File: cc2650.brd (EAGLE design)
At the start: 50.8 x 22.9 mm, 22 parts, among them IC1 TPS73133DBVR, IC4 CC2650MODAMOHR, SW1 SPST_TACT-KMR2, SW3 SPST_TACT-KMR2

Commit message: changed resistor values for LEDS.
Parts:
- LED2: value RED -> GREEN
- R2: value 470 -> 715
- R3: value 470 -> 787
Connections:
- removed net N$4: JP2.1
- net DIO5_TDO: now also JP2.1
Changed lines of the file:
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@@
 <attribute name="VALUE" x="19.134" y="20.334" size="0.4064" layer="27" rot="R180"/>
 </element>
-<element name="R3" library="adafruit" package="R1206" value="470" x="15.8115" y="12.065" rot="MR90">
+<element name="R3" library="adafruit" package="R1206" value="787" x="15.8115" y="12.065" rot="MR90">
 <attribute name="MF" value="" x="15.8115" y="12.065" size="1.778" layer="28" rot="MR90" display="off"/>
 <attribute name="MPN" value="CR1206-FX-4700ELF" x="15.8115" y="12.065" size="1.778" layer="28" rot="MR90" display="off"/>
@@
 <element name="CN1" library="adafruit" package="JST-PH-2-THM-RA" value="" x="10.795" y="16.51"/>
 <element name="MS1" library="wing_modified" package="FEATHERWING_DIM" value="FEATHERWING_NODIM" x="0" y="0"/>
-<element name="R2" library="adafruit" package="R1206" value="470" x="18.415" y="12.065" rot="MR90">
+<element name="R2" library="adafruit" package="R1206" value="715" x="18.415" y="12.065" rot="MR90">
 <attribute name="MF" value="" x="36.195" y="12.065" size="1.778" layer="28" rot="MR90" display="off"/>
 <attribute name="MPN" value="CR1206-FX-4700ELF" x="36.195" y="12.065" size="1.778" layer="28" rot="MR90" display="off"/>
 <attribute name="OC_NEWARK" value="06X5194" x="36.195" y="12.065" size="1.778" layer="28" rot="MR90" display="off"/>
 </element>
-<element name="LED2" library="adafruit" package="CHIPLED_1206" value="RED" x="18.415" y="12.065" rot="R180">
+<element name="LED2" library="adafruit" package="CHIPLED_1206" value="GREEN" x="18.415" y="12.065" rot="R180">
 <attribute name="MF" value="" x="29.845" y="-6.35" size="1.778" layer="27" rot="R180" display="off"/>
 <attribute name="MPN" value="HSMC-C150" x="29.845" y="-6.35" size="1.778" layer="27" rot="R180" display="off"/>
@@
 <contactref element="JTAG_CONNECTOR" pad="6"/>
 <contactref element="MS1" pad="5"/>
+<contactref element="JP2" pad="1"/>
 <wire x1="31.242" y1="13.922" x2="34.084" y2="13.7935" width="0" layer="19" extent="1-1"/>
-<wire x1="16.51" y1="1.27" x2="31.242" y2="13.922" width="0" layer="19" extent="1-1"/>
+<wire x1="18.415" y1="5.08" x2="31.242" y2="13.922" width="0" layer="19" extent="1-1"/>
+<wire x1="16.51" y1="1.27" x2="18.415" y2="5.08" width="0" layer="19" extent="1-1"/>
 </signal>
 <signal name="DIO6_TDI">
@@
 <wire x1="18.415" y1="7.62" x2="18.415" y2="10.643" width="0" layer="19" extent="16-16"/>
 </signal>
-<signal name="N$4">
-<contactref element="JP2" pad="1"/>
-</signal>
 </signals>

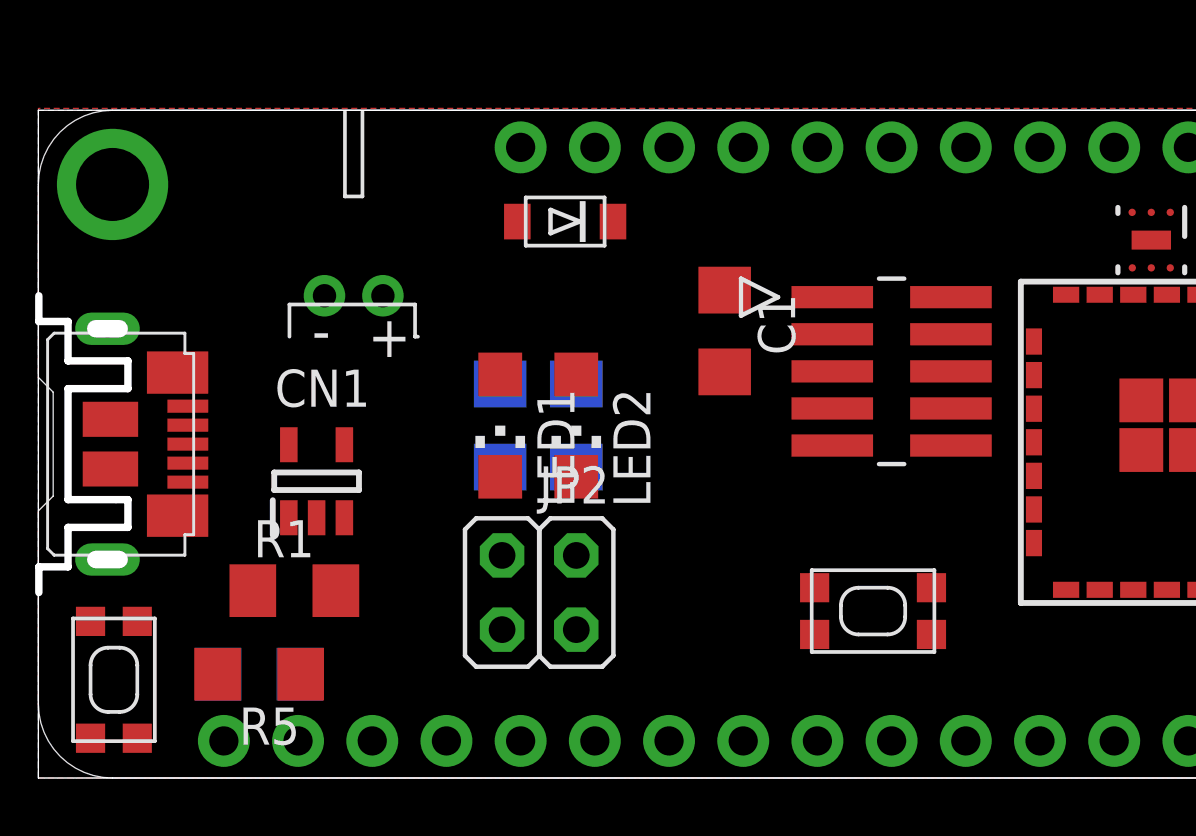
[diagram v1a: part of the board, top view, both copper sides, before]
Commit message: changed power circuitry
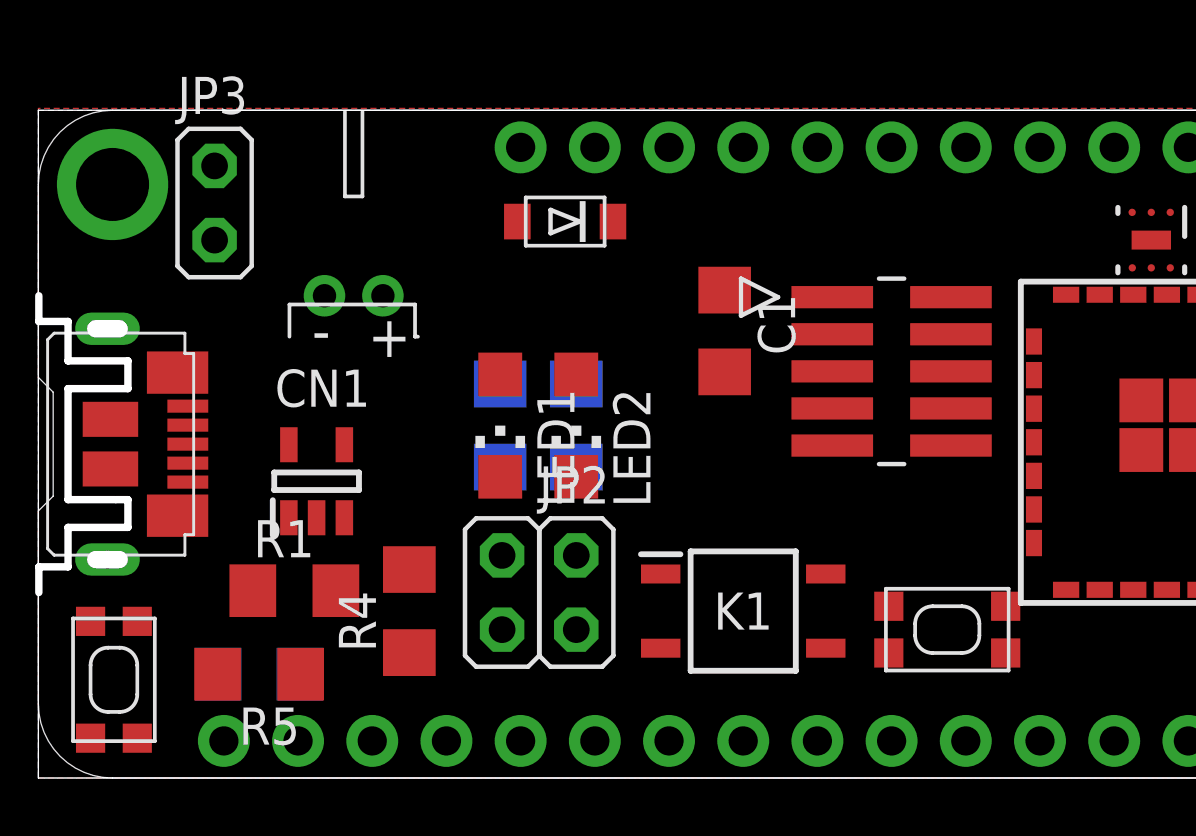
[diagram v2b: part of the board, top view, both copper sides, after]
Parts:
- added JP3: PWR_LED, jumper:JP1M
- added K1: CPC1117N, CPC1117N:SOP254P610X218-4N
- added R4: 150, adafruit:R1206
- moved SW3 2.62 mm to (31.1, 5.08)
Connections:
- new net N$4: D2.C, IC1.1, K1.4, R1.1
- new net N$5: IC1.5, JP3.1
- new net N$6: K1.1, R4.1
- net GND: now also K1.2
- net VBAT: now also K1.3; no longer D2.A
- net VBUS: now also D2.A, R4.2; no longer D2.C, IC1.1, R1.1
- net VCC: now also JP3.2; no longer IC1.5
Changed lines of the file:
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@@
 <attribute name="SUPPLIER_NAME" value="RS" x="9.525" y="10.16" size="1.778" layer="27" rot="R90" display="off"/>
 </element>
-<element name="SW3" library="adafruit" package="KMR2" value="SPST_TACT-KMR2" x="28.575" y="5.715" smashed="yes">
-<attribute name="MF" value="" x="2.54" y="48.26" size="1.778" layer="27" display="off"/>
-<attribute name="MPN" value="KMR241G LFS" x="2.54" y="48.26" size="1.778" layer="27" display="off"/>
-<attribute name="OC_NEWARK" value="58M7854" x="2.54" y="48.26" size="1.778" layer="27" display="off"/>
+<element name="SW3" library="adafruit" package="KMR2" value="SPST_TACT-KMR2" x="31.115" y="5.08" smashed="yes">
+<attribute name="MF" value="" x="5.08" y="47.625" size="1.778" layer="27" display="off"/>
+<attribute name="MPN" value="KMR241G LFS" x="5.08" y="47.625" size="1.778" layer="27" display="off"/>
+<attribute name="OC_NEWARK" value="58M7854" x="5.08" y="47.625" size="1.778" layer="27" display="off"/>
 </element>
 <element name="OPT3001" library="OPT3001" package="DNP0006A" value="Value" x="38.1" y="18.415" smashed="yes" rot="R270">
@@
 <attribute name="MPN" value="2211S-02G" x="-3.175" y="18.415" size="1.778" layer="27" display="off"/>
 <attribute name="OC_NEWARK" value="08N6744" x="-3.175" y="18.415" size="1.778" layer="27" display="off"/>
+</element>
+<element name="K1" library="CPC1117N" package="SOP254P610X218-4N" value="CPC1117N" x="24.13" y="5.715">
+<attribute name="3D_PACKAGE" value="" x="24.13" y="5.715" size="1.778" layer="27" display="off"/>
+<attribute name="ALLIED_NUMBER" value="" x="24.13" y="5.715" size="1.778" layer="27" display="off"/>
+<attribute name="DESCRIPTION" value="SPST-NC Solid State Relay Solder 150 mA rms/mA dc Surface Mount, DC MOSFET" x="24.13" y="5.715" size="1.778" layer="27" display="off"/>
+<attribute name="HEIGHT" value="2.184mm" x="24.13" y="5.715" size="1.778" layer="27" display="off"/>
+<attribute name="MANUFACTURER_NAME" value="IXYS SEMICONDUCTOR" x="24.13" y="5.715" size="1.778" layer="27" display="off"/>
+<attribute name="MANUFACTURER_PART_NUMBER" value="CPC1117N" x="24.13" y="5.715" size="1.778" layer="27" display="off"/>
+<attribute name="OTHER_PART_NUMBER" value="" x="24.13" y="5.715" size="1.778" layer="27" display="off"/>
+<attribute name="RS_PART_NUMBER" value="9061039" x="24.13" y="5.715" size="1.778" layer="27" display="off"/>
+<attribute name="SUPPLIER_NAME" value="RS" x="24.13" y="5.715" size="1.778" layer="27" display="off"/>
+</element>
+<element name="R4" library="adafruit" package="R1206" value="150" x="12.7" y="5.715" rot="R90">
+<attribute name="MF" value="" x="12.7" y="5.715" size="1.778" layer="27" rot="R90" display="off"/>
+<attribute name="MPN" value="CR1206-FX-4700ELF" x="12.7" y="5.715" size="1.778" layer="27" rot="R90" display="off"/>
+<attribute name="OC_NEWARK" value="06X5194" x="12.7" y="5.715" size="1.778" layer="27" rot="R90" display="off"/>
+</element>
+<element name="JP3" library="jumper" package="JP1M" value="PWR_LED" x="6.0325" y="19.685">
+<attribute name="MF" value="" x="6.0325" y="19.685" size="1.778" layer="27" display="off"/>
+<attribute name="MPN" value="2211S-02G" x="6.0325" y="19.685" size="1.778" layer="27" display="off"/>
+<attribute name="OC_NEWARK" value="08N6744" x="6.0325" y="19.685" size="1.778" layer="27" display="off"/>
 </element>
 </elements>
@@
 <contactref element="MS1" pad="16"/>
 <contactref element="LED2" pad="C"/>
+<contactref element="K1" pad="2"/>
 <wire x1="42.084" y1="16.5435" x2="44.384" y2="16.5435" width="0" layer="19" extent="1-1"/>
 <wire x1="38.1" y1="18.415" x2="42.084" y2="16.5435" width="0" layer="19" extent="1-1"/>
@@
 <wire x1="44.384" y1="6.4435" x2="39.459" y2="11.2285" width="0" layer="19" extent="1-1"/>
 <wire x1="44.45" y1="1.27" x2="44.384" y2="6.4435" width="0" layer="19" extent="1-1"/>
-<wire x1="30.575" y1="6.515" x2="37.759" y2="11.2285" width="0" layer="19" extent="1-1"/>
-<wire x1="26.575" y1="6.515" x2="30.575" y2="6.515" width="0" layer="19" extent="1-1"/>
-<wire x1="27.178" y1="11.382" x2="26.575" y2="6.515" width="0" layer="19" extent="1-1"/>
+<wire x1="33.115" y1="5.88" x2="37.759" y2="11.2285" width="0" layer="19" extent="1-1"/>
+<wire x1="29.115" y1="5.88" x2="33.115" y2="5.88" width="0" layer="19" extent="1-1"/>
+<wire x1="27.178" y1="11.382" x2="29.115" y2="5.88" width="0" layer="19" extent="1-1"/>
 <wire x1="27.178" y1="13.922" x2="27.178" y2="11.382" width="0" layer="19" extent="1-1"/>
 <wire x1="27.178" y1="15.192" x2="27.178" y2="13.922" width="0" layer="19" extent="1-1"/>
-<wire x1="23.495" y1="13.9035" x2="27.178" y2="15.192" width="0" layer="19" extent="1-1"/>
-<wire x1="18.415" y1="10.315" x2="27.178" y2="11.382" width="0" layer="19" extent="1-1"/>
+<wire x1="23.495" y1="13.9035" x2="27.178" y2="13.922" width="0" layer="19" extent="1-1"/>
+<wire x1="18.415" y1="10.315" x2="23.495" y2="13.9035" width="0" layer="19" extent="1-1"/>
 <wire x1="15.8115" y1="10.315" x2="18.415" y2="10.315" width="0" layer="19" extent="1-1"/>
 <wire x1="10.475" y1="11.41" x2="15.8115" y2="10.315" width="0" layer="19" extent="1-1"/>
@@
 <wire x1="1.7865" y1="5.3625" x2="8.9565" y2="3.556" width="0" layer="19" extent="1-16"/>
 <wire x1="1.7865" y1="1.3625" x2="1.7865" y2="5.3625" width="0" layer="19" extent="1-1"/>
+<wire x1="21.305" y1="4.445" x2="1.7865" y2="1.3625" width="0" layer="19" extent="1-1"/>
 </signal>
 <signal name="NRESET">
@@
 <contactref element="SW3" pad="4"/>
 <contactref element="MS1" pad="9"/>
-<wire x1="30.575" y1="4.915" x2="39.784" y2="6.4435" width="0" layer="19" extent="1-1"/>
-<wire x1="26.575" y1="4.915" x2="30.575" y2="4.915" width="0" layer="19" extent="1-1"/>
-<wire x1="26.67" y1="1.27" x2="26.575" y2="4.915" width="0" layer="19" extent="1-1"/>
+<wire x1="33.115" y1="4.28" x2="39.784" y2="6.4435" width="0" layer="19" extent="1-1"/>
+<wire x1="29.115" y1="4.28" x2="33.115" y2="4.28" width="0" layer="19" extent="1-1"/>
+<wire x1="26.67" y1="1.27" x2="29.115" y2="4.28" width="0" layer="19" extent="1-1"/>
 </signal>
 <signal name="DIO13">
@@
 <contactref element="IC4" pad="23"/>
 <contactref element="JTAG_CONNECTOR" pad="1"/>
-<contactref element="IC1" pad="5"/>
 <contactref element="OPT3001" pad="2"/>
 <contactref element="OPT3001" pad="1"/>
@@
 <contactref element="JP1" pad="1"/>
 <contactref element="MS1" pad="2"/>
+<contactref element="JP3" pad="2"/>
 <wire x1="40.869" y1="18.796" x2="40.869" y2="19.177" width="0" layer="19" extent="1-16"/>
 <wire x1="38.75" y1="19.365" x2="40.869" y2="19.177" width="0" layer="19" extent="1-16"/>
@@
 <wire x1="40.934" y1="6.4435" x2="40.869" y2="18.796" width="0" layer="19" extent="1-1"/>
 <wire x1="42.084" y1="6.4435" x2="40.934" y2="6.4435" width="0" layer="19" extent="1-1"/>
-<wire x1="8.575" y1="11.41" x2="23.495" y2="16.7035" width="0" layer="19" extent="1-1"/>
-<wire x1="8.9785" y1="3.556" x2="8.575" y2="11.41" width="0" layer="19" extent="1-1"/>
+<wire x1="15.875" y1="5.08" x2="23.495" y2="16.7035" width="0" layer="19" extent="1-1"/>
+<wire x1="8.9785" y1="3.556" x2="15.875" y2="5.08" width="0" layer="19" extent="1-1"/>
 <wire x1="8.89" y1="1.27" x2="8.9785" y2="3.556" width="0" layer="19" extent="1-1"/>
-<wire x1="15.875" y1="5.08" x2="8.9785" y2="3.556" width="0" layer="19" extent="1-1"/>
+<wire x1="6.0325" y1="20.955" x2="8.89" y2="1.27" width="0" layer="19" extent="1-1"/>
 </signal>
 <signal name="VBAT">
-<contactref element="D2" pad="A"/>
 <contactref element="CN1" pad="1"/>
 <contactref element="MS1" pad="28"/>
-<wire x1="16.3965" y1="19.05" x2="16.51" y2="21.59" width="0" layer="19" extent="1-1"/>
-<wire x1="11.795" y1="16.51" x2="16.3965" y2="19.05" width="0" layer="19" extent="1-1"/>
+<contactref element="K1" pad="3"/>
+<wire x1="11.795" y1="16.51" x2="16.51" y2="21.59" width="0" layer="19" extent="1-1"/>
+<wire x1="26.955" y1="4.445" x2="11.795" y2="16.51" width="0" layer="19" extent="1-1"/>
 </signal>
 <signal name="VBUS" class="2">
 <contactref element="USB101" pad="VBUS"/>
-<contactref element="IC1" pad="1"/>
-<contactref element="D2" pad="C"/>
-<contactref element="R1" pad="1"/>
 <contactref element="MS1" pad="26"/>
-<wire x1="19.6715" y1="19.05" x2="21.59" y2="21.59" width="0" layer="19" extent="1-1"/>
-<wire x1="8.575" y1="8.91" x2="19.6715" y2="19.05" width="0" layer="19" extent="1-1"/>
-<wire x1="7.341" y1="6.4135" x2="8.575" y2="8.91" width="0" layer="19" extent="1-1"/>
-<wire x1="5.116" y1="10.13" x2="8.575" y2="8.91" width="0" layer="19" extent="1-1"/>
+<contactref element="D2" pad="A"/>
+<contactref element="R4" pad="2"/>
+<wire x1="16.3965" y1="19.05" x2="21.59" y2="21.59" width="0" layer="19" extent="1-1"/>
+<wire x1="5.116" y1="10.13" x2="16.3965" y2="19.05" width="0" layer="19" extent="1-1"/>
+<wire x1="12.7" y1="7.137" x2="5.116" y2="10.13" width="0" layer="19" extent="1-1"/>
 </signal>
 <signal name="EN">
@@
 <wire x1="18.415" y1="7.62" x2="18.415" y2="10.643" width="0" layer="19" extent="16-16"/>
 </signal>
+<signal name="N$4">
+<contactref element="K1" pad="4"/>
+<contactref element="IC1" pad="1"/>
+<contactref element="R1" pad="1"/>
+<contactref element="D2" pad="C"/>
+<wire x1="8.575" y1="8.91" x2="19.6715" y2="19.05" width="0" layer="19" extent="1-1"/>
+<wire x1="7.341" y1="6.4135" x2="8.575" y2="8.91" width="0" layer="19" extent="1-1"/>
+<wire x1="26.955" y1="6.985" x2="7.341" y2="6.4135" width="0" layer="19" extent="1-1"/>
+</signal>
+<signal name="N$6">
+<contactref element="K1" pad="1"/>
+<contactref element="R4" pad="1"/>
+<wire x1="21.305" y1="6.985" x2="12.7" y2="4.293" width="0" layer="19" extent="1-1"/>
+</signal>
+<signal name="N$5">
+<contactref element="IC1" pad="5"/>
+<contactref element="JP3" pad="1"/>
+<wire x1="8.575" y1="11.41" x2="6.0325" y2="18.415" width="0" layer="19" extent="1-1"/>
+</signal>
 </signals>

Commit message: Changed power circuitry. Added TI ESD Suppresor.
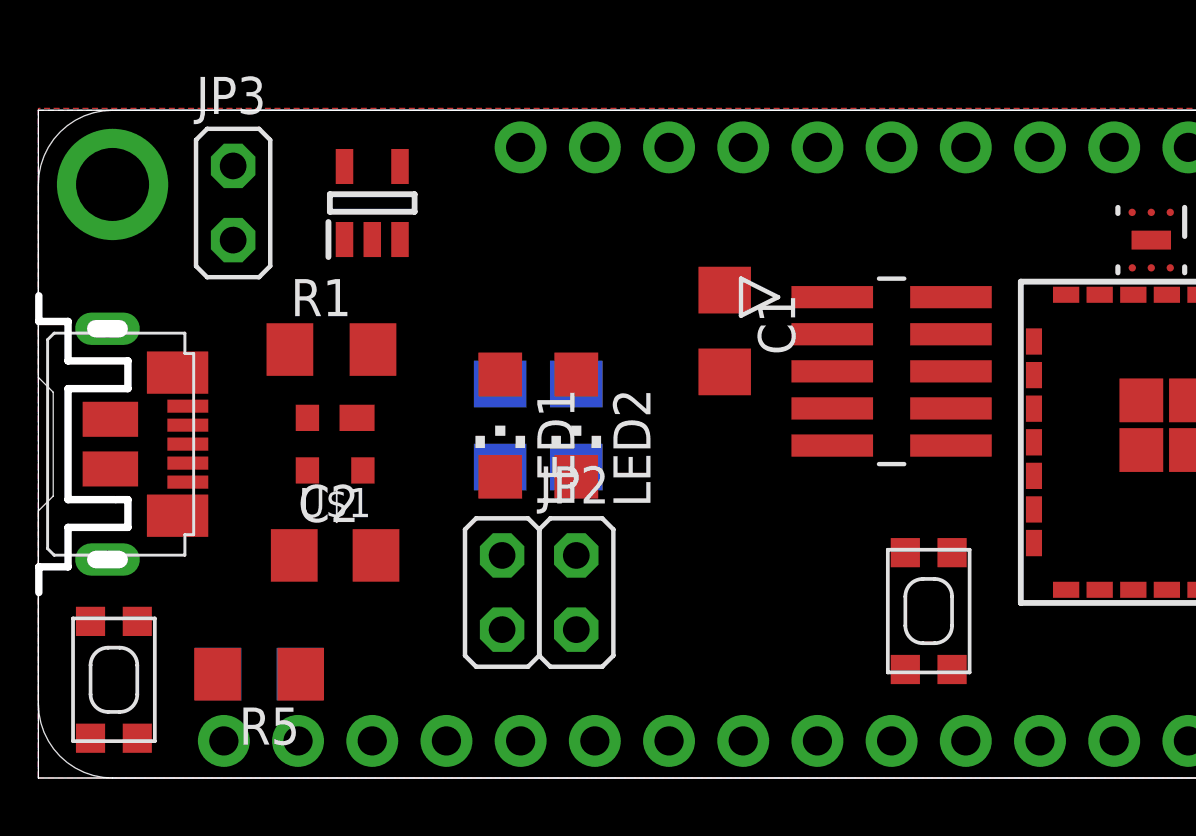
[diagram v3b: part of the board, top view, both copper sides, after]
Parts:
- removed CN1: (no value), adafruit:JST-PH-2-THM-RA
- removed D2: (no value), adafruit:SOD-123FL
- removed K1: CPC1117N, CPC1117N:SOP254P610X218-4N
- removed R4: 150, adafruit:R1206
- added C2: 0.1u, adafruit:C1206
- added U$1: TPD2E001, AMP_Ruler-LT1370:SOT-143
- moved IC1 9.71 mm to (11.4, 19.7)
- moved R1 8.35 mm to (10.0, 14.7)
- moved SW3 0.90 mm to (30.5, 5.71), turned to 90 degrees
- moved JP3 0.64 mm to (6.67, 19.7)
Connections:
- removed net N$4: D2.C, IC1.1, K1.4, R1.1
- removed net N$6: K1.1, R4.1
- new net D+: U$1.2, USB101.D+
- new net D-: U$1.3, USB101.D-
- net GND: now also C2.2, U$1.1; no longer CN1.2, K1.2
- net VBAT: no longer CN1.1, K1.3
- net VBUS: now also C2.1, IC1.1, R1.1, U$1.4; no longer D2.A, R4.2
